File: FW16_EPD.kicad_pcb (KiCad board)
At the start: 2 copper layers, 67.8 x 131 mm, 67 parts, among them J1 Conn_01x02, J2 Framework Input Module Connec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, J3 FH34SRJ-24S-0.5SH, J4 FH34SRJ-6S-0.5SH, Q1 DMG3404L, Q2 SSM3J338R, U1 RP2040, U2 W25Q128JVP, U3 MCP9808_DFN, Y1 12.000 MHz ABM8-272-T3

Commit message: update date
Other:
- board text added: "(c) arthomnix 2024 2024-11-29 r1.0"
- board text removed: "(c) arthomnix 2024 2024-10-03 r1.0"
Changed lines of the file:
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@@
 	(title_block
 		(title "Framework 16 Touchscreen EPD Input Module")
-		(date "2024-10-03")
+		(date "2024-11-29")
 		(rev "1.0")
 	)
@@
 		)
 	)
-	(gr_text "(c) arthomnix 2024\n2024-10-03 r1.0"
+	(gr_text "(c) arthomnix 2024\n2024-11-29 r1.0"
 		(at 121.83 37.652696 0)
 		(layer "F.SilkS")

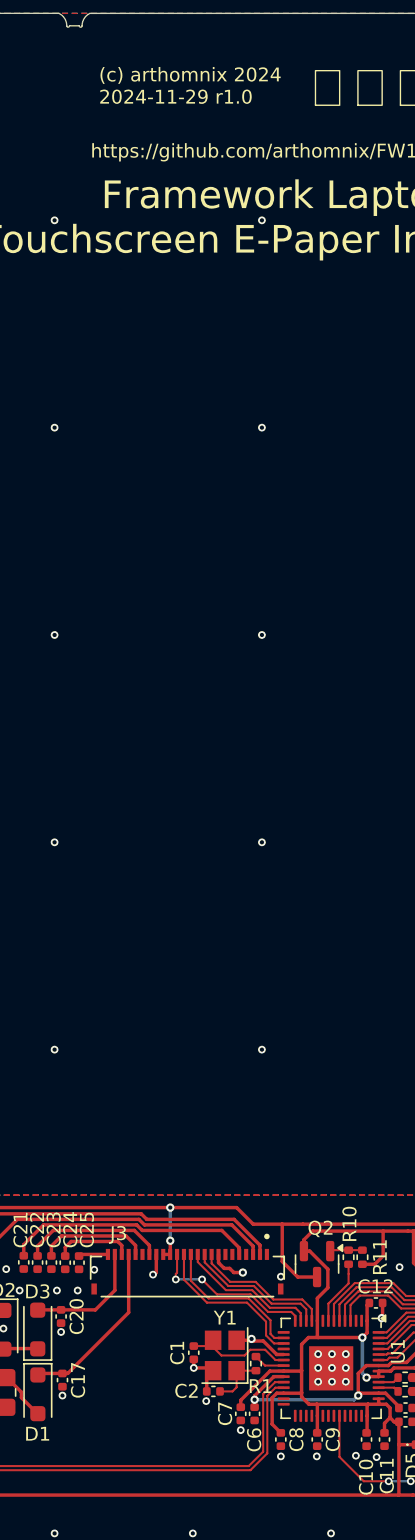
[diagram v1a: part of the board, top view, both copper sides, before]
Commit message: move crystal for better clearance with FFC
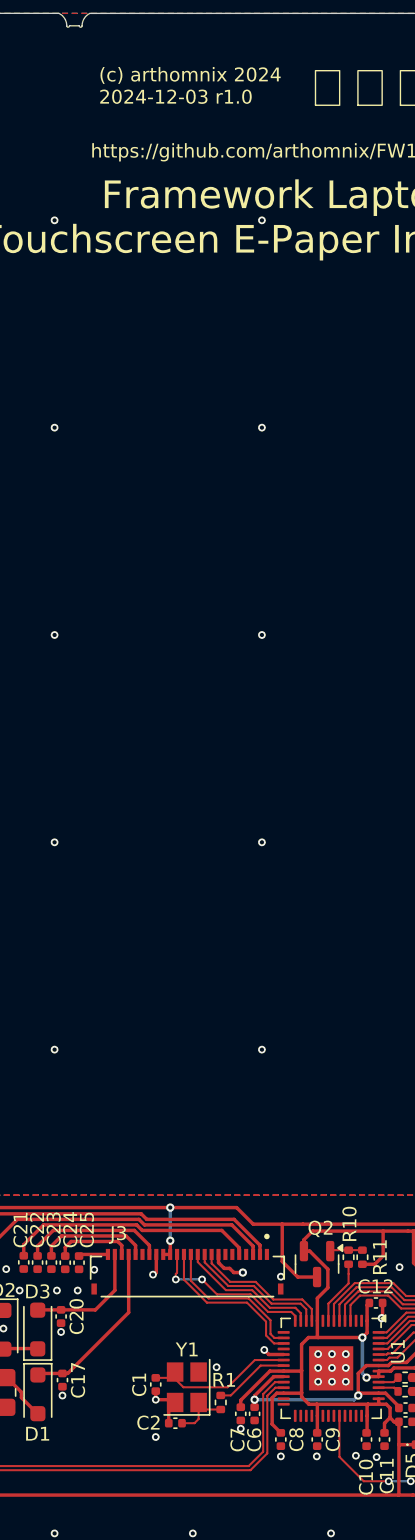
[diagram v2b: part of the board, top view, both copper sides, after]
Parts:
- moved R1 3.79 mm to (130.7, 131.5)
- moved C2 3.59 mm to (127.4, 133.0)
- moved Y1 3.59 mm to (128.2, 130.4)
- moved C1 3.59 mm to (126.0, 130.2)
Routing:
- net Net-(U1-XOUT): track 2.27 -> 5.45 mm
- net Net-(U1-XIN): track 8.70 -> 11.8 mm
- net GND: track 33.0 -> 30.6 mm, vias 89 -> 90
- net Net-(C2-Pad2): track 3.92 -> 4.48 mm
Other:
- board text added: "(c) arthomnix 2024 2024-12-03 r1.0"
- board text removed: "(c) arthomnix 2024 2024-11-29 r1.0"
